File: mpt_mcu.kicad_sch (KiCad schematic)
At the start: 11 parts, among them SW2 KMR421GULCLFS, SW3 KMR421GULCLFS, U4 ESP32-S3-WROOM-1-N4R2

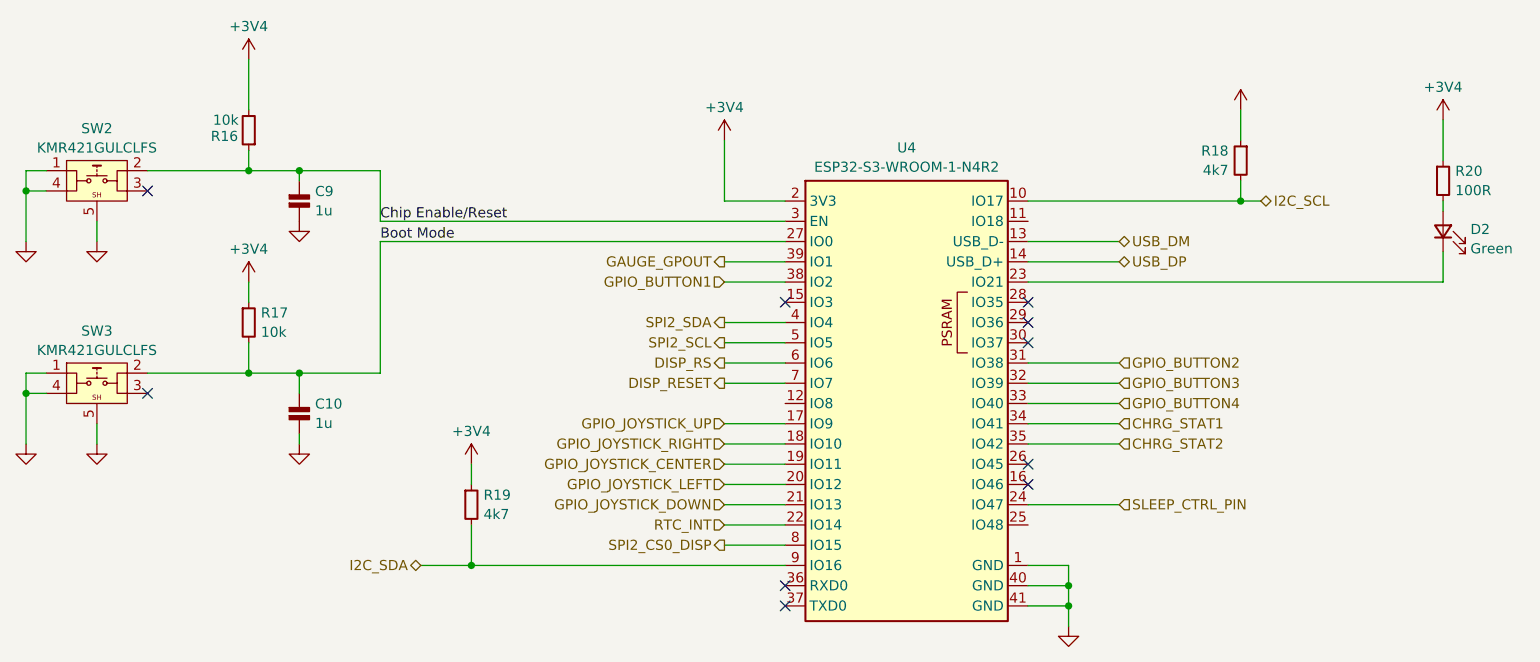
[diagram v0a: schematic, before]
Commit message: Replace LED Driver Remove maybe buzzer
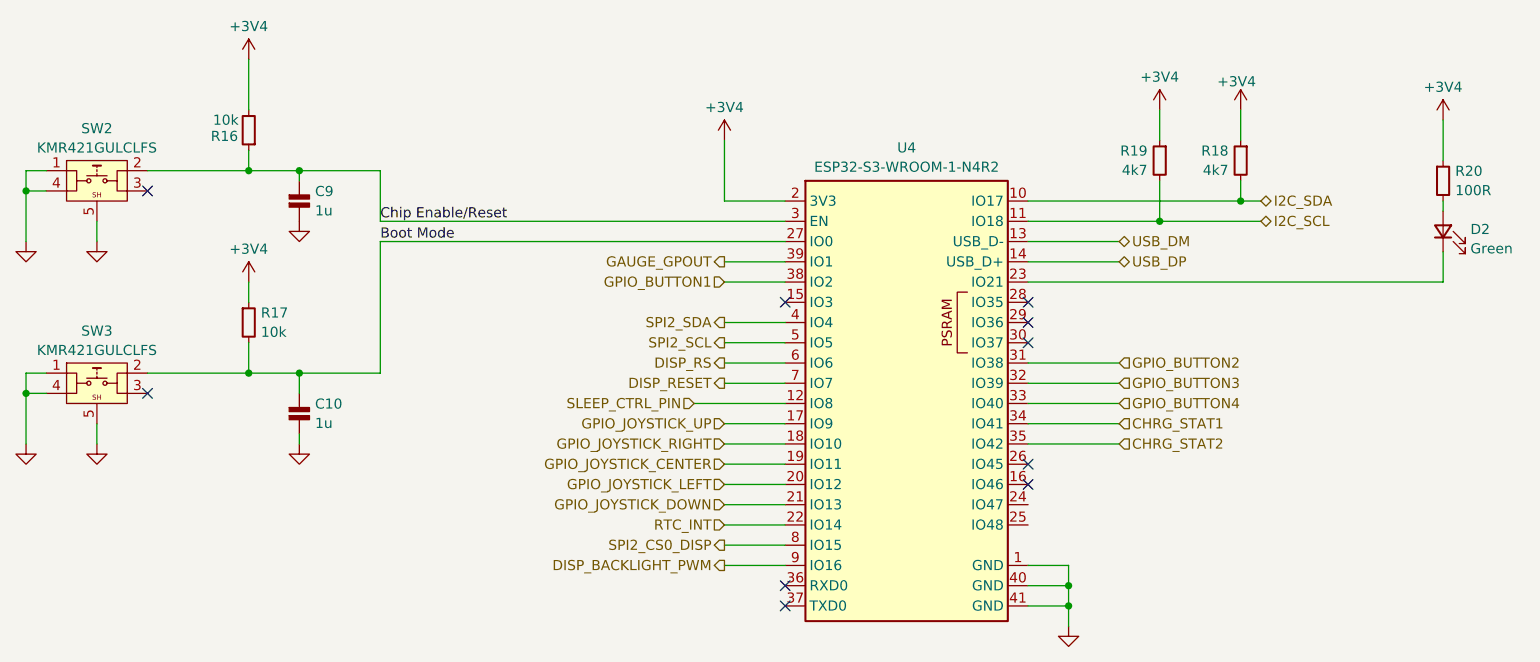
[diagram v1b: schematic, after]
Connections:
- net I2C_SCL: now also R19.2, U4.11 (IO18); no longer R18.2, U4.10 (IO17)
- net I2C_SDA: now also R18.2, U4.10 (IO17); no longer R19.2, U4.9 (IO16)
- net SLEEP_CTRL_PIN: now also U4.12 (IO8); no longer U4.24 (IO47)
- new net DISP_BACKLIGHT_PWM: U4.9 (IO16)

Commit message: PCB Layout Connecting
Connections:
- net GPIO_BUTTON1: now also U4.18 (IO10); no longer U4.38 (IO2)
- net GPIO_BUTTON2: now also U4.19 (IO11); no longer U4.31 (IO38)
- net GPIO_BUTTON3: now also U4.20 (IO12); no longer U4.32 (IO39)
- net GPIO_BUTTON4: now also U4.21 (IO13); no longer U4.33 (IO40)
- net GPIO_JOYSTICK_CENTER: now also U4.25 (IO48); no longer U4.19 (IO11)
- net GPIO_JOYSTICK_DOWN: now also U4.22 (IO14); no longer U4.21 (IO13)
- net GPIO_JOYSTICK_LEFT: now also U4.31 (IO38); no longer U4.20 (IO12)
- net GPIO_JOYSTICK_RIGHT: now also U4.23 (IO21); no longer U4.18 (IO10)
- net GPIO_JOYSTICK_UP: now also U4.24 (IO47); no longer U4.17 (IO9)
- net RTC_INT: now also U4.17 (IO9); no longer U4.22 (IO14)
- net at D2.2 (K): now also U4.38 (IO2); no longer U4.23 (IO21)
